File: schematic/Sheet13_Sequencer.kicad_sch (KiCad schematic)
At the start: 11 parts, among them U13A TPS7H3014-SP, U13B TPS7H3014-SP

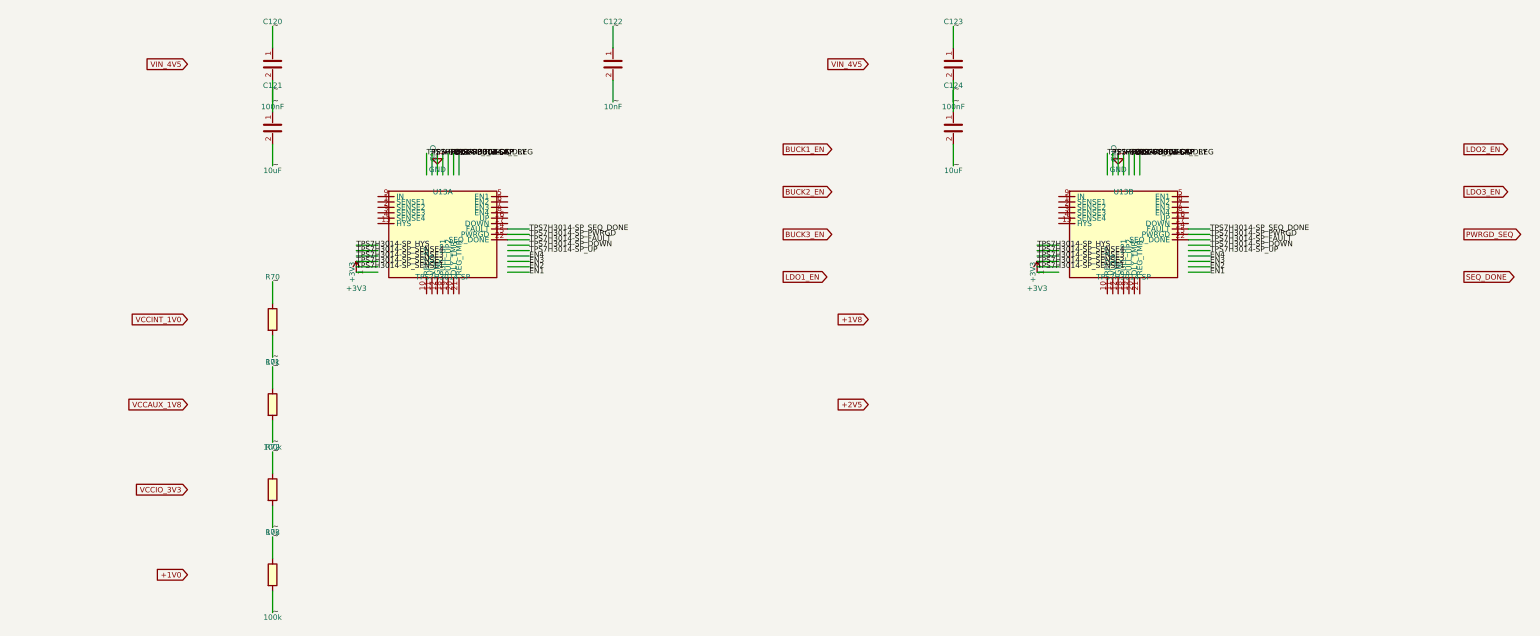
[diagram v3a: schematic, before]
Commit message: Fix KiCad schematic wiring: Y-inversion bug + all 891 pins connected
- Fixed critical Y-axis inversion bug: KiCad inverts Y when placing
  symbols (lib Y + schematic Y = abs Y is WRONG; correct: abs Y = sym Y - lib Y)
- This caused ALL wires to connect to wrong pins (e.g., CS label connected
  to BG pin instead of CS pin)
- Verified with netlist: 0 unconnected nets, all pin functions correct
- Fixed wire direction for angle 90/270 (swapped due to Y-inversion)
- 891 pin connections across 15 sheets, all 17 sheets export without errors
- Netlist verification: CS→E8, BG→C3, INA+→A4, CLK+→F1, JESD pairs correct

Co-Authored-By: opencode <noreply@opencode.ai>
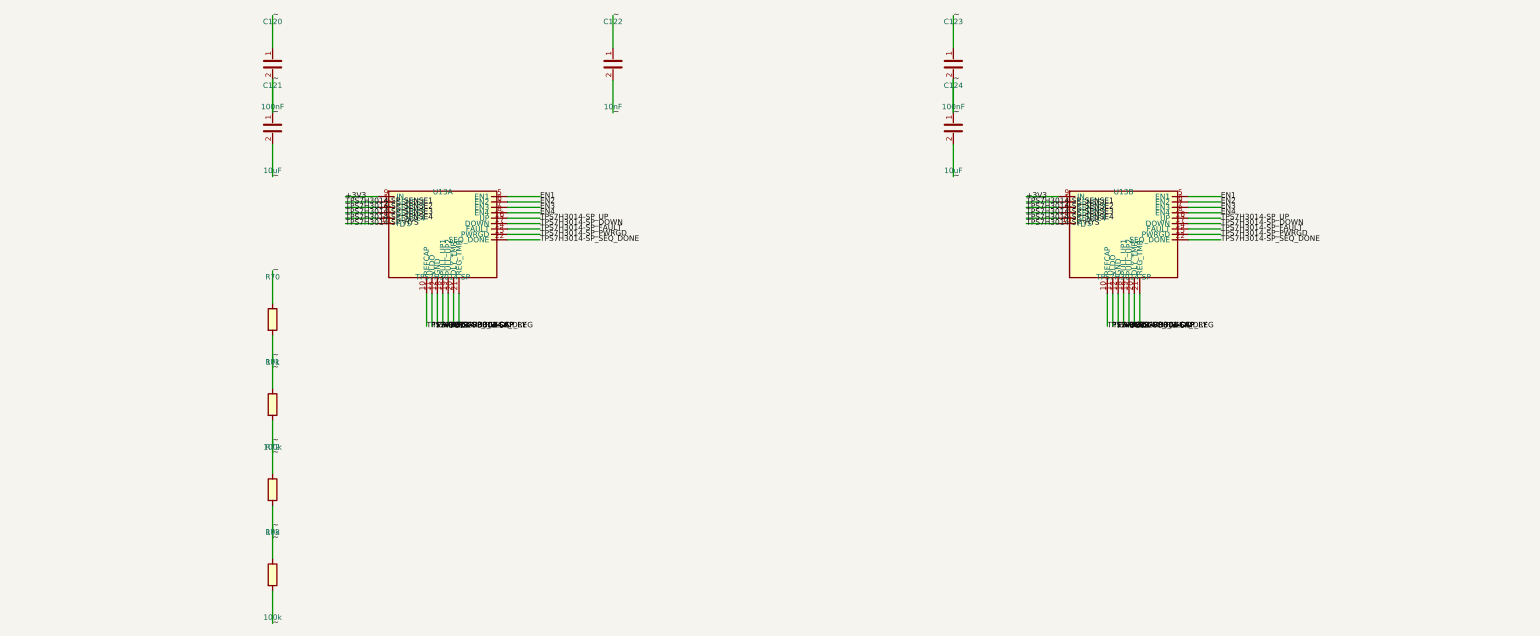
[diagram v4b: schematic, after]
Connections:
- net +3V3: now also U13A.18 (PULL_UP1), U13A.19 (PULL_UP2), U13A.9 (IN), U13B.18 (PULL_UP1), U13B.19 (PULL_UP2), U13B.9 (IN)
- net EN1: now also U13A.5 (EN1), U13B.5 (EN1)
- net EN2: now also U13A.6 (EN2), U13B.6 (EN2)
- net EN3: now also U13A.7 (EN3), U13B.7 (EN3)
- net EN4: now also U13A.8 (EN4), U13B.8 (EN4)
- net GND: now also U13A.12 (GND), U13B.12 (GND)
- net TPS7H3014-SP_DLY: now also U13A.20 (DLY_TMR), U13B.20 (DLY_TMR)
- net TPS7H3014-SP_DOWN: now also U13A.17 (DOWN), U13B.17 (DOWN)
- net TPS7H3014-SP_FAULT: now also U13A.14 (FAULT), U13B.14 (FAULT); no longer U13A.22 (SEQ_DONE), U13B.22 (SEQ_DONE)
- net TPS7H3014-SP_HYS: now also U13A.13 (HYS), U13B.13 (HYS)
- net TPS7H3014-SP_REFCAP: now also U13A.10 (REFCAP), U13B.10 (REFCAP)
- net TPS7H3014-SP_REG: now also U13A.21 (REG_TMR), U13B.21 (REG_TMR)
- net TPS7H3014-SP_SENSE1: now also U13A.1 (SENSE1), U13B.1 (SENSE1)
- net TPS7H3014-SP_SENSE2: now also U13A.2 (SENSE2), U13B.2 (SENSE2)
- net TPS7H3014-SP_SENSE3: now also U13A.3 (SENSE3), U13B.3 (SENSE3)
- net TPS7H3014-SP_SENSE4: now also U13A.4 (SENSE4), U13B.4 (SENSE4)
- net TPS7H3014-SP_SEQ_DONE: now also U13A.22 (SEQ_DONE), U13B.22 (SEQ_DONE); no longer U13A.14 (FAULT), U13B.14 (FAULT)
- net TPS7H3014-SP_UP: now also U13A.16 (UP), U13B.16 (UP)
- net TPS7H3014-SP_VLDO: now also U13A.11 (VLDO), U13B.11 (VLDO)

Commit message: fix: replace wire stubs with labels-only to prevent power net shorts
Labels placed directly at pin endpoints eliminate wire overlap that
caused BGA power pins (VA11, VA19, VD11, AGND, DGND) to merge into
a single net. Verified via netlist: GND=52, +1V0_ANA=12, +1V9_ANA=12,
+1V1_DIG=10 nodes (all correct per datasheet pin mapping).
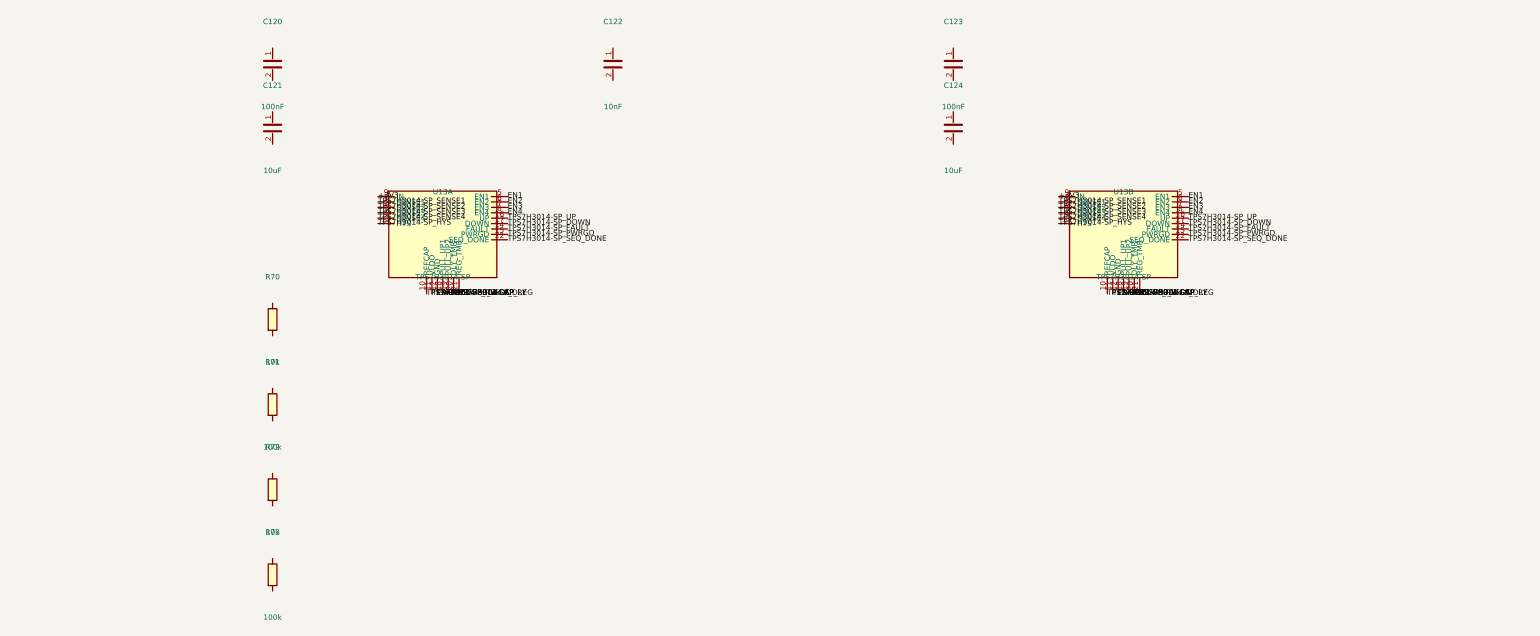
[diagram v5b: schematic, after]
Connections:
- removed net ~: C120.1, C120.2, C121.1, C121.2, C122.1, C122.2, C123.1, C123.2, C124.1, C124.2, R70.1, R70.2, R71.1, R71.2, R72.1, R72.2, R73.1, R73.2

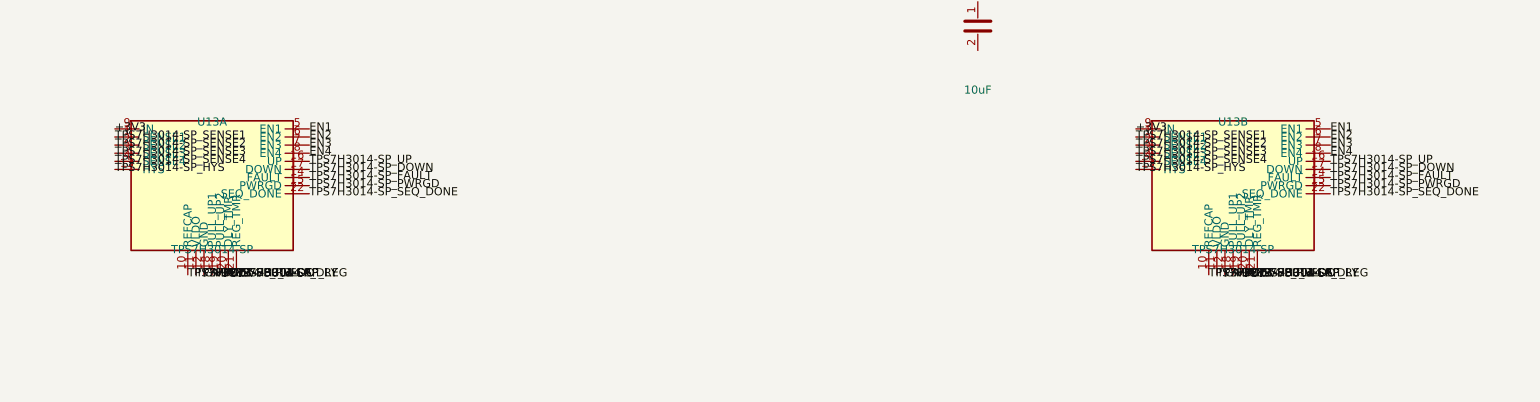
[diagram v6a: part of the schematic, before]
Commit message: fix: isolate ISL70003ASEH buck pins, fix LMX_SYNC collision, NC pins, connector pin names
- ISL70003ASEH pins now use ref prefix (U6_LX1 vs U7_LX1) to prevent shorts
- Buck SYNC pins separated from LMX_SYNC (power sync ≠ PLL sync)
- NC pins properly skipped (unconnected)
- Connector PIN_1..PIN_6 use ref prefix (J1_PIN_1 vs J2_PIN_1)
- Fixed annotation warnings in Sheet13 (C_dev→C125, R_dev→R74, U_TPS7H→U14)
- Regenerated all PDFs and SVGs
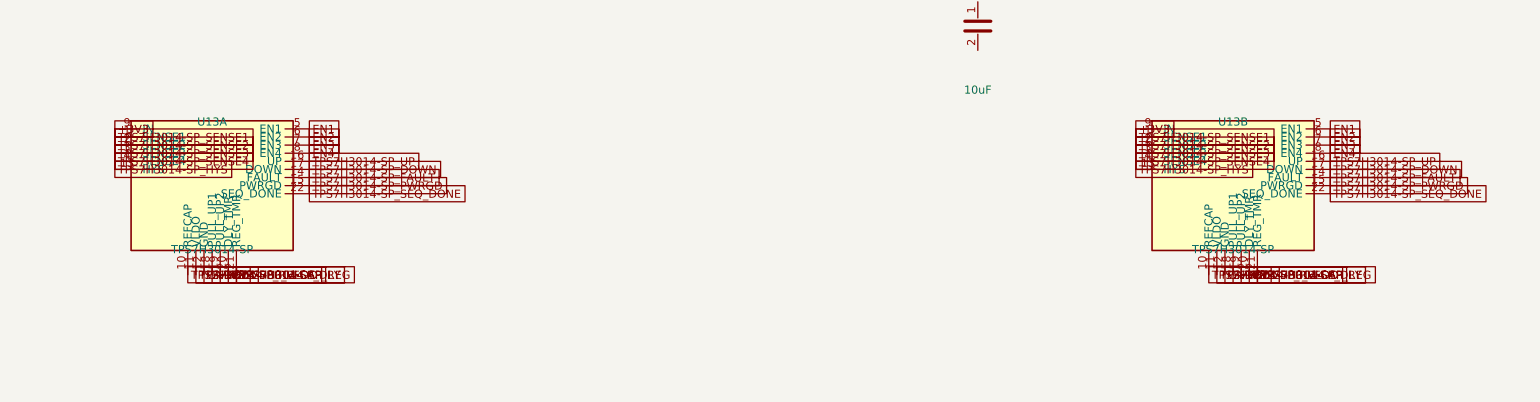
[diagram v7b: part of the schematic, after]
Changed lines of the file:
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@@
     (pin "2")
   )
-  (label "+3V3" (at 104.7600 71.1100 0) (effects (font (size 1.27 1.27))))
-  (label "TPS7H3014-SP_SENSE1" (at 104.7600 72.3800 0) (effects (font (size 1.27 1.27))))
-  (label "TPS7H3014-SP_SENSE2" (at 104.7600 73.6500 0) (effects (font (size 1.27 1.27))))
-  (label "TPS7H3014-SP_SENSE3" (at 104.7600 74.9200 0) (effects (font (size 1.27 1.27))))
-  (label "TPS7H3014-SP_SENSE4" (at 104.7600 76.1900 0) (effects (font (size 1.27 1.27))))
-  (label "TPS7H3014-SP_HYS" (at 104.7600 77.4600 0) (effects (font (size 1.27 1.27))))
-  (label "EN1" (at 135.2400 71.1100 0) (effects (font (size 1.27 1.27))))
-  (label "EN2" (at 135.2400 72.3800 0) (effects (font (size 1.27 1.27))))
-  (label "EN3" (at 135.2400 73.6500 0) (effects (font (size 1.27 1.27))))
-  (label "EN4" (at 135.2400 74.9200 0) (effects (font (size 1.27 1.27))))
-  (label "TPS7H3014-SP_UP" (at 135.2400 76.1900 0) (effects (font (size 1.27 1.27))))
-  (label "TPS7H3014-SP_DOWN" (at 135.2400 77.4600 0) (effects (font (size 1.27 1.27))))
-  (label "TPS7H3014-SP_FAULT" (at 135.2400 78.7300 0) (effects (font (size 1.27 1.27))))
-  (label "TPS7H3014-SP_PWRGD" (at 135.2400 80.0000 0) (effects (font (size 1.27 1.27))))
-  (label "TPS7H3014-SP_SEQ_DONE" (at 135.2400 81.2700 0) (effects (font (size 1.27 1.27))))
-  (label "TPS7H3014-SP_REFCAP" (at 116.1900 93.9700 0) (effects (font (size 1.27 1.27))))
-  (label "TPS7H3014-SP_VLDO" (at 117.4600 93.9700 0) (effects (font (size 1.27 1.27))))
-  (label "GND" (at 118.7300 93.9700 0) (effects (font (size 1.27 1.27))))
-  (label "+3V3" (at 120.0000 93.9700 0) (effects (font (size 1.27 1.27))))
-  (label "+3V3" (at 121.2700 93.9700 0) (effects (font (size 1.27 1.27))))
-  (label "TPS7H3014-SP_DLY" (at 122.5400 93.9700 0) (effects (font (size 1.27 1.27))))
-  (label "TPS7H3014-SP_REG" (at 123.8100 93.9700 0) (effects (font (size 1.27 1.27))))
-  (label "+3V3" (at 264.7600 71.1100 0) (effects (font (size 1.27 1.27))))
-  (label "TPS7H3014-SP_SENSE1" (at 264.7600 72.3800 0) (effects (font (size 1.27 1.27))))
-  (label "TPS7H3014-SP_SENSE2" (at 264.7600 73.6500 0) (effects (font (size 1.27 1.27))))
-  (label "TPS7H3014-SP_SENSE3" (at 264.7600 74.9200 0) (effects (font (size 1.27 1.27))))
-  (label "TPS7H3014-SP_SENSE4" (at 264.7600 76.1900 0) (effects (font (size 1.27 1.27))))
-  (label "TPS7H3014-SP_HYS" (at 264.7600 77.4600 0) (effects (font (size 1.27 1.27))))
-  (label "EN1" (at 295.2400 71.1100 0) (effects (font (size 1.27 1.27))))
-  (label "EN2" (at 295.2400 72.3800 0) (effects (font (size 1.27 1.27))))
-  (label "EN3" (at 295.2400 73.6500 0) (effects (font (size 1.27 1.27))))
-  (label "EN4" (at 295.2400 74.9200 0) (effects (font (size 1.27 1.27))))
-  (label "TPS7H3014-SP_UP" (at 295.2400 76.1900 0) (effects (font (size 1.27 1.27))))
-  (label "TPS7H3014-SP_DOWN" (at 295.2400 77.4600 0) (effects (font (size 1.27 1.27))))
-  (label "TPS7H3014-SP_FAULT" (at 295.2400 78.7300 0) (effects (font (size 1.27 1.27))))
-  (label "TPS7H3014-SP_PWRGD" (at 295.2400 80.0000 0) (effects (font (size 1.27 1.27))))
-  (label "TPS7H3014-SP_SEQ_DONE" (at 295.2400 81.2700 0) (effects (font (size 1.27 1.27))))
-  (label "TPS7H3014-SP_REFCAP" (at 276.1900 93.9700 0) (effects (font (size 1.27 1.27))))
-  (label "TPS7H3014-SP_VLDO" (at 277.4600 93.9700 0) (effects (font (size 1.27 1.27))))
-  (label "GND" (at 278.7300 93.9700 0) (effects (font (size 1.27 1.27))))
-  (label "+3V3" (at 280.0000 93.9700 0) (effects (font (size 1.27 1.27))))
-  (label "+3V3" (at 281.2700 93.9700 0) (effects (font (size 1.27 1.27))))
-  (label "TPS7H3014-SP_DLY" (at 282.5400 93.9700 0) (effects (font (size 1.27 1.27))))
-  (label "TPS7H3014-SP_REG" (at 283.8100 93.9700 0) (effects (font (size 1.27 1.27))))
+  (global_label "+3V3" (at 104.7600 71.1100 0) (effects (font (size 1.27 1.27))))
+  (global_label "TPS7H3014-SP_SENSE1" (at 104.7600 72.3800 0) (effects (font (size 1.27 1.27))))
+  (global_label "TPS7H3014-SP_SENSE2" (at 104.7600 73.6500 0) (effects (font (size 1.27 1.27))))
+  (global_label "TPS7H3014-SP_SENSE3" (at 104.7600 74.9200 0) (effects (font (size 1.27 1.27))))
+  (global_label "TPS7H3014-SP_SENSE4" (at 104.7600 76.1900 0) (effects (font (size 1.27 1.27))))
+  (global_label "TPS7H3014-SP_HYS" (at 104.7600 77.4600 0) (effects (font (size 1.27 1.27))))
+  (global_label "EN1" (at 135.2400 71.1100 0) (effects (font (size 1.27 1.27))))
+  (global_label "EN2" (at 135.2400 72.3800 0) (effects (font (size 1.27 1.27))))
+  (global_label "EN3" (at 135.2400 73.6500 0) (effects (font (size 1.27 1.27))))
+  (global_label "EN4" (at 135.2400 74.9200 0) (effects (font (size 1.27 1.27))))
+  (global_label "TPS7H3014-SP_UP" (at 135.2400 76.1900 0) (effects (font (size 1.27 1.27))))
+  (global_label "TPS7H3014-SP_DOWN" (at 135.2400 77.4600 0) (effects (font (size 1.27 1.27))))
+  (global_label "TPS7H3014-SP_FAULT" (at 135.2400 78.7300 0) (effects (font (size 1.27 1.27))))
+  (global_label "TPS7H3014-SP_PWRGD" (at 135.2400 80.0000 0) (effects (font (size 1.27 1.27))))
+  (global_label "TPS7H3014-SP_SEQ_DONE" (at 135.2400 81.2700 0) (effects (font (size 1.27 1.27))))
+  (global_label "TPS7H3014-SP_REFCAP" (at 116.1900 93.9700 0) (effects (font (size 1.27 1.27))))
+  (global_label "TPS7H3014-SP_VLDO" (at 117.4600 93.9700 0) (effects (font (size 1.27 1.27))))
+  (global_label "GND" (at 118.7300 93.9700 0) (effects (font (size 1.27 1.27))))
+  (global_label "+3V3" (at 120.0000 93.9700 0) (effects (font (size 1.27 1.27))))
+  (global_label "+3V3" (at 121.2700 93.9700 0) (effects (font (size 1.27 1.27))))
+  (global_label "TPS7H3014-SP_DLY" (at 122.5400 93.9700 0) (effects (font (size 1.27 1.27))))
+  (global_label "TPS7H3014-SP_REG" (at 123.8100 93.9700 0) (effects (font (size 1.27 1.27))))
+  (global_label "+3V3" (at 264.7600 71.1100 0) (effects (font (size 1.27 1.27))))
+  (global_label "TPS7H3014-SP_SENSE1" (at 264.7600 72.3800 0) (effects (font (size 1.27 1.27))))
+  (global_label "TPS7H3014-SP_SENSE2" (at 264.7600 73.6500 0) (effects (font (size 1.27 1.27))))
+  (global_label "TPS7H3014-SP_SENSE3" (at 264.7600 74.9200 0) (effects (font (size 1.27 1.27))))
+  (global_label "TPS7H3014-SP_SENSE4" (at 264.7600 76.1900 0) (effects (font (size 1.27 1.27))))
+  (global_label "TPS7H3014-SP_HYS" (at 264.7600 77.4600 0) (effects (font (size 1.27 1.27))))
+  (global_label "EN1" (at 295.2400 71.1100 0) (effects (font (size 1.27 1.27))))
+  (global_label "EN2" (at 295.2400 72.3800 0) (effects (font (size 1.27 1.27))))
+  (global_label "EN3" (at 295.2400 73.6500 0) (effects (font (size 1.27 1.27))))
+  (global_label "EN4" (at 295.2400 74.9200 0) (effects (font (size 1.27 1.27))))
+  (global_label "TPS7H3014-SP_UP" (at 295.2400 76.1900 0) (effects (font (size 1.27 1.27))))
+  (global_label "TPS7H3014-SP_DOWN" (at 295.2400 77.4600 0) (effects (font (size 1.27 1.27))))
+  (global_label "TPS7H3014-SP_FAULT" (at 295.2400 78.7300 0) (effects (font (size 1.27 1.27))))
+  (global_label "TPS7H3014-SP_PWRGD" (at 295.2400 80.0000 0) (effects (font (size 1.27 1.27))))
+  (global_label "TPS7H3014-SP_SEQ_DONE" (at 295.2400 81.2700 0) (effects (font (size 1.27 1.27))))
+  (global_label "TPS7H3014-SP_REFCAP" (at 276.1900 93.9700 0) (effects (font (size 1.27 1.27))))
+  (global_label "TPS7H3014-SP_VLDO" (at 277.4600 93.9700 0) (effects (font (size 1.27 1.27))))
+  (global_label "GND" (at 278.7300 93.9700 0) (effects (font (size 1.27 1.27))))
+  (global_label "+3V3" (at 280.0000 93.9700 0) (effects (font (size 1.27 1.27))))
+  (global_label "+3V3" (at 281.2700 93.9700 0) (effects (font (size 1.27 1.27))))
+  (global_label "TPS7H3014-SP_DLY" (at 282.5400 93.9700 0) (effects (font (size 1.27 1.27))))
+  (global_label "TPS7H3014-SP_REG" (at 283.8100 93.9700 0) (effects (font (size 1.27 1.27))))
   (sheet_instances (path "/" (page "1")))
 )

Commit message: feat: connect ALL passive components and fix clock routing
- Added PASSIVE_TOPOLOGY dict mapping 139 passives to their nets
- Passive pin endpoints now get global_labels (was 0 connected, now 138)
- R38 intentionally GND-GND (RECAL_EN pull-down)
- Fixed LMK clock output mapping: CLKout0→ADC_CLK_P, CLKout2→FPGA_REFCLK_P, etc.
- Fixed TPS7H5001-SP SYNC pin collision with LMX_SYNC
- Total connections: 867 pins (up from 641)
- Cross-sheet nets: 52
- Power rails: VIN(33), +3V3(98), GND(228) all with decoupling
- JESD204C: U1↔U2 on 4 lanes ✓
- SPI: U1↔U2↔U3↔U4 ✓
- Clock: LMK→ADC (CLK+SYSREF), LMK→FPGA (REF+SPW) ✓
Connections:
- net GND: now also C120.2, C121.2, C122.2, C123.2, C124.2, R71.2, R73.2
- net VIN_4V5: now reaches C121.1
- net VIN_4V5: now also C120.1, C123.1, C124.1
- net VCCINT_1V0: now reaches R70.1
- net U13A_S2: now reaches R70.2
- net U13A_S2: now also R71.1
- net U13A_S3: now reaches R73.1
- net U13A_S3: now also R72.2
- net VCCAUX_1V8: now reaches R72.1
- net U13A_VLDO: now reaches C122.1
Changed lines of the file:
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@@
   (global_label "TPS7H3014-SP_DLY" (at 282.5400 93.9700 0) (effects (font (size 1.27 1.27))))
   (global_label "TPS7H3014-SP_REG" (at 283.8100 93.9700 0) (effects (font (size 1.27 1.27))))
+  (global_label "VIN_4V5" (at 80.0000 36.1900 0) (effects (font (size 1.27 1.27))))
+  (global_label "GND" (at 80.0000 43.8100 0) (effects (font (size 1.27 1.27))))
+  (global_label "VIN_4V5" (at 80.0000 51.1900 0) (effects (font (size 1.27 1.27))))
+  (global_label "GND" (at 80.0000 58.8100 0) (effects (font (size 1.27 1.27))))
+  (global_label "VCCINT_1V0" (at 80.0000 96.1900 0) (effects (font (size 1.27 1.27))))
+  (global_label "U13A_S2" (at 80.0000 103.8100 0) (effects (font (size 1.27 1.27))))
+  (global_label "U13A_S2" (at 80.0000 116.1900 0) (effects (font (size 1.27 1.27))))
+  (global_label "GND" (at 80.0000 123.8100 0) (effects (font (size 1.27 1.27))))
+  (global_label "VCCAUX_1V8" (at 80.0000 136.1900 0) (effects (font (size 1.27 1.27))))
+  (global_label "U13A_S3" (at 80.0000 143.8100 0) (effects (font (size 1.27 1.27))))
+  (global_label "U13A_S3" (at 80.0000 156.1900 0) (effects (font (size 1.27 1.27))))
+  (global_label "GND" (at 80.0000 163.8100 0) (effects (font (size 1.27 1.27))))
+  (global_label "U13A_VLDO" (at 160.0000 36.1900 0) (effects (font (size 1.27 1.27))))
+  (global_label "GND" (at 160.0000 43.8100 0) (effects (font (size 1.27 1.27))))
+  (global_label "VIN_4V5" (at 240.0000 36.1900 0) (effects (font (size 1.27 1.27))))
+  (global_label "GND" (at 240.0000 43.8100 0) (effects (font (size 1.27 1.27))))
+  (global_label "VIN_4V5" (at 240.0000 51.1900 0) (effects (font (size 1.27 1.27))))
+  (global_label "GND" (at 240.0000 58.8100 0) (effects (font (size 1.27 1.27))))
   (sheet_instances (path "/" (page "1")))
 )
